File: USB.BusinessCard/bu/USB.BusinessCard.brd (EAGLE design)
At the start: 30.1 x 80 mm, 5 parts

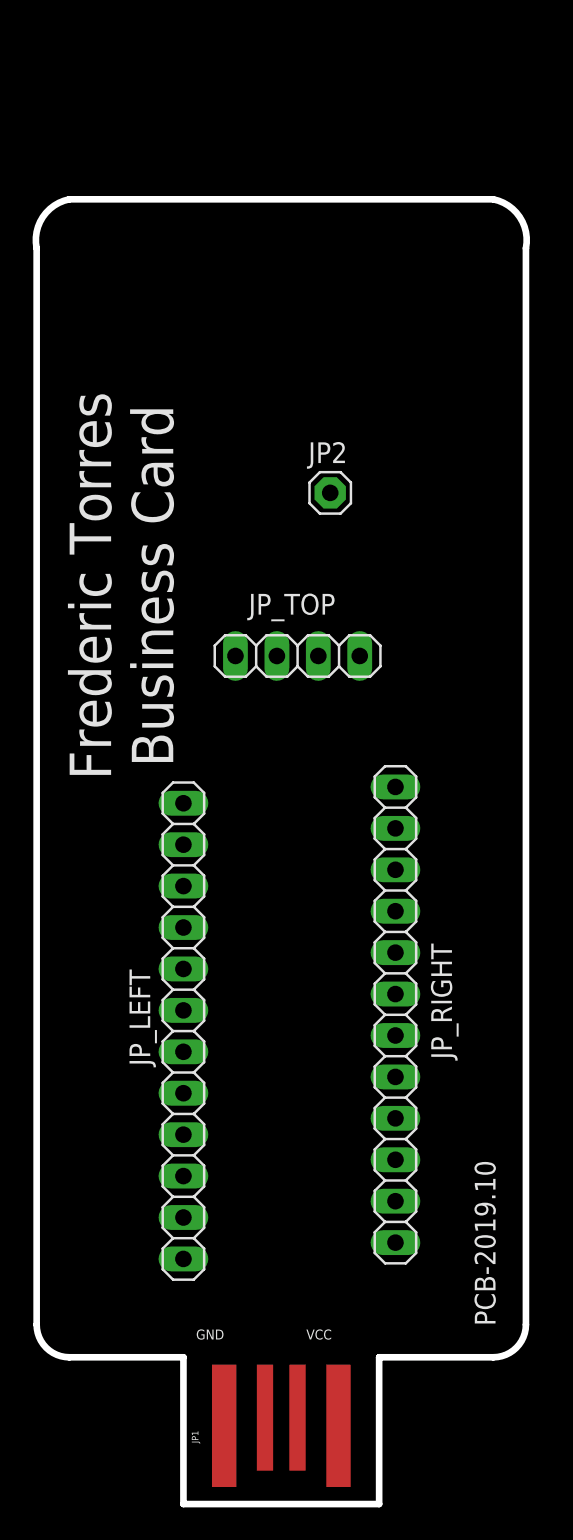
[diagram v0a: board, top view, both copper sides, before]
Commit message: Write firmware for Usb Business Card
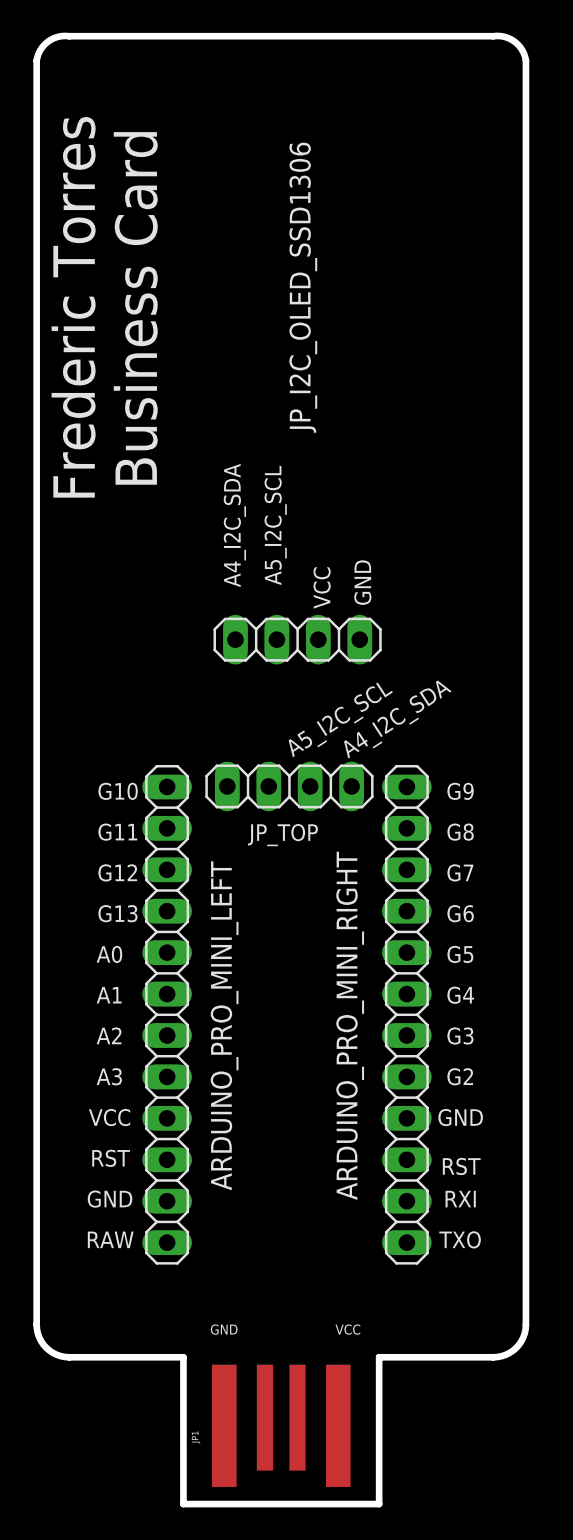
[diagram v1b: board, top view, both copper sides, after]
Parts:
- removed JP2: (no value), adafruit:1X01
- removed JP_LEFT, JP_RIGHT: (no value), adafruit:1X12
- added ARDUINO_PRO_MINI_LEFT, ARDUINO_PRO_MINI_RIGHT: (no value), adafruit:1X12
- added JP_I2C_OLED_SSD1306: (no value), pinhead:1X04
- moved JP_TOP 8.02 mm to (15.5, 44.0)
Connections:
- net A0: now also ARDUINO_PRO_MINI_LEFT.5; no longer JP_LEFT.5
- net A1: now also ARDUINO_PRO_MINI_LEFT.6; no longer JP_LEFT.6
- net A2: now also ARDUINO_PRO_MINI_LEFT.7; no longer JP_LEFT.7
- net A3: now also ARDUINO_PRO_MINI_LEFT.8; no longer JP_LEFT.8
- net A4_I2C_SDA: now also JP_I2C_OLED_SSD1306.4; no longer JP2.1
- net A5_I2C_SCL: now also JP_I2C_OLED_SSD1306.3
- net G10: now also ARDUINO_PRO_MINI_LEFT.1; no longer JP_LEFT.1
- net G11: now also ARDUINO_PRO_MINI_LEFT.2; no longer JP_LEFT.2
- net G12: now also ARDUINO_PRO_MINI_LEFT.3; no longer JP_LEFT.3
- net G13: now also ARDUINO_PRO_MINI_LEFT.4; no longer JP_LEFT.4
- net G2: now also ARDUINO_PRO_MINI_RIGHT.8; no longer JP_RIGHT.8
- net G3: now also ARDUINO_PRO_MINI_RIGHT.7; no longer JP_RIGHT.7
- net G4: now also ARDUINO_PRO_MINI_RIGHT.6; no longer JP_RIGHT.6
- net G5: now also ARDUINO_PRO_MINI_RIGHT.5; no longer JP_RIGHT.5
- net G6: now also ARDUINO_PRO_MINI_RIGHT.4; no longer JP_RIGHT.4
- net G7: now also ARDUINO_PRO_MINI_RIGHT.3; no longer JP_RIGHT.3
- net G8: now also ARDUINO_PRO_MINI_RIGHT.2; no longer JP_RIGHT.2
- net G9: now also ARDUINO_PRO_MINI_RIGHT.1; no longer JP_RIGHT.1
- net GND: now also ARDUINO_PRO_MINI_LEFT.11, ARDUINO_PRO_MINI_RIGHT.9, JP_I2C_OLED_SSD1306.1; no longer JP_LEFT.11, JP_RIGHT.9
- net RAW: now also ARDUINO_PRO_MINI_LEFT.12; no longer JP_LEFT.12
- net RST: now also ARDUINO_PRO_MINI_LEFT.10, ARDUINO_PRO_MINI_RIGHT.10; no longer JP_LEFT.10, JP_RIGHT.10
- net RXI: now also ARDUINO_PRO_MINI_RIGHT.11; no longer JP_RIGHT.11
- net TXO: now also ARDUINO_PRO_MINI_RIGHT.12; no longer JP_RIGHT.12
- net VCC: now also ARDUINO_PRO_MINI_LEFT.9, JP_I2C_OLED_SSD1306.2; no longer JP_LEFT.9
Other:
- board size 30.1 x 80 mm -> 30 x 90 mm
- board text added: "A0"
- board text added: "A1"
- board text added: "A2"
- board text added: "A3"
- board text added: "A4_I2C_SDA"
- board text added: "A5_I2C_SCL"
- board text added: "G10"
- board text added: "G11"
- board text added: "G12"
- board text added: "G13"
- board text added: "G2"
- board text added: "G3"
- board text added: "G4"
- board text added: "G5"
- board text added: "G6"
- board text added: "G7"
- board text added: "G8"
- board text added: "G9"
- board text added: "PCB c 2019.10"
- board text added: "RAW"
- board text added: "RST"
- board text added: "RXI"
- board text added: "TXO"
- board text removed: "Nusbio"
- board text removed: "PCB-2019.10"

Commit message: Update firmware for Usb Business Card
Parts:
- added JP_PROGRAMMING: (no value), adafruit:1X06
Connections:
- removed net G11: ARDUINO_PRO_MINI_LEFT.2
- removed net G12: ARDUINO_PRO_MINI_LEFT.3
- removed net G13: ARDUINO_PRO_MINI_LEFT.4
- new net G11_MOSI: ARDUINO_PRO_MINI_LEFT.2, JP_PROGRAMMING.6
- new net G12_MISO: ARDUINO_PRO_MINI_LEFT.3, JP_PROGRAMMING.5
- new net G13_SCK: ARDUINO_PRO_MINI_LEFT.4, JP_PROGRAMMING.4
- net GND: now also JP_PROGRAMMING.1
- net RST: now also JP_PROGRAMMING.3
- net VCC: now also JP_PROGRAMMING.2
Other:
- board text added: "G11_MOSI"
- board text added: "G12_MISO"
- board text added: "G13_SCK"
- board text removed: "G11"
- board text removed: "G12"
- board text removed: "G13"
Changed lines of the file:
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@@
 <layer number="23" name="tOrigins" color="15" fill="1" visible="yes" active="yes"/>
 <layer number="24" name="bOrigins" color="15" fill="1" visible="yes" active="yes"/>
-<layer number="25" name="tNames" color="7" fill="1" visible="no" active="yes"/>
-<layer number="26" name="bNames" color="7" fill="1" visible="yes" active="yes"/>
+<layer number="25" name="tNames" color="7" fill="1" visible="yes" active="yes"/>
+<layer number="26" name="bNames" color="7" fill="1" visible="no" active="yes"/>
 <layer number="27" name="tValues" color="7" fill="1" visible="yes" active="yes"/>
 <layer number="28" name="bValues" color="7" fill="1" visible="yes" active="yes"/>
@@
 <text x="11.5" y="10.7" size="0.6096" layer="25" rot="R180" align="center">GND</text>
 <text x="19.1" y="10.7" size="0.6096" layer="25" rot="R180" align="center">VCC</text>
-<text x="4.2" y="73.3" size="2.54" layer="25" rot="R90" align="center">Frederic Torres
+<text x="26.2" y="73.3" size="2.54" layer="25" rot="R90" align="center">Frederic Torres
 Business Card</text>
 <text x="15.5" y="20" size="2.54" layer="26" rot="MR270" align="center">MadeInTheUSB.net</text>
@@
 <text x="4.5" y="31.2" size="1.016" layer="25" rot="R180" align="center">A1</text>
 <text x="4.5" y="33.7" size="1.016" layer="25" rot="R180" align="center">A0</text>
-<text x="5" y="36.2" size="1.016" layer="25" rot="R180" align="center">G13</text>
-<text x="5" y="38.7" size="1.016" layer="25" rot="R180" align="center">G12</text>
-<text x="5" y="41.2" size="1.016" layer="25" rot="R180" align="center">G11</text>
+<text x="3.5" y="36.2" size="1.016" layer="25" rot="R180" align="center">G13_SCK</text>
+<text x="3.5" y="38.7" size="0.8128" layer="25" rot="R180" align="center">G12_MISO</text>
+<text x="3.5" y="41.2" size="0.8128" layer="25" rot="R180" align="center">G11_MOSI</text>
 <text x="5" y="43.7" size="1.016" layer="25" rot="R180" align="center">G10</text>
 <text x="26" y="26.2" size="1.016" layer="25" rot="R180" align="center">G2</text>
@@
 <text x="26" y="16.2" size="1.016" layer="25" rot="R180" align="center">TXO</text>
 <text x="4.5" y="16.2" size="1.016" layer="25" rot="R180" align="center">RAW</text>
+<text x="7.5" y="65.7" size="1.016" layer="25" rot="R180" align="center">GND</text>
+<text x="7.5" y="68.2" size="1.016" layer="25" rot="R180" align="center">VCC</text>
+<text x="7.5" y="70.7" size="1.016" layer="25" rot="R180" align="center">RST</text>
+<text x="9" y="73.2" size="1.016" layer="25" rot="R180" align="center">G13_SCK</text>
+<text x="9.5" y="75.7" size="1.016" layer="25" rot="R180" align="center">G12_MISO</text>
+<text x="9.5" y="78.2" size="1.016" layer="25" rot="R180" align="center">G11_MOSI</text>
 </plain>
 <attributes>
@@
 <attribute name="VALUE" x="21.08" y="56.175" size="1.27" layer="27" rot="R180"/>
 </element>
+<element name="JP_PROGRAMMING" library="adafruit" package="1X06" value="" x="4" y="72" smashed="yes" rot="R90">
+<attribute name="NAME" x="2.1712" y="64.3038" size="1.016" layer="25" ratio="10" rot="R90"/>
+<attribute name="VALUE" x="7.175" y="64.38" size="1.27" layer="27" rot="R90"/>
+</element>
 </elements>
 <signals>
@@
 <contactref element="ARDUINO_PRO_MINI_RIGHT" pad="9"/>
 <contactref element="JP_I2C_OLED_SSD1306" pad="1"/>
+<contactref element="JP_PROGRAMMING" pad="1"/>
 <wire x1="22.7" y1="23.65" x2="19.81" y2="53" width="0" layer="19" extent="1-1"/>
 <wire x1="8" y1="18.57" x2="22.7" y2="23.65" width="0" layer="19" extent="1-1"/>
 <wire x1="11.5" y1="4.8" x2="8" y2="18.57" width="0" layer="19" extent="1-1"/>
+<wire x1="4" y1="65.65" x2="11.5" y2="4.8" width="0" layer="19" extent="1-1"/>
 </signal>
 <signal name="VCC">
@@
 <contactref element="ARDUINO_PRO_MINI_LEFT" pad="9"/>
 <contactref element="JP_I2C_OLED_SSD1306" pad="2"/>
+<contactref element="JP_PROGRAMMING" pad="2"/>
 <wire x1="8" y1="23.65" x2="17.27" y2="53" width="0" layer="19" extent="1-1"/>
 <wire x1="18.5" y1="4.8" x2="8" y2="23.65" width="0" layer="19" extent="1-1"/>
+<wire x1="4" y1="68.19" x2="18.5" y2="4.8" width="0" layer="19" extent="1-1"/>
 </signal>
 <signal name="RAW">
@@
 <contactref element="ARDUINO_PRO_MINI_LEFT" pad="10"/>
 <contactref element="ARDUINO_PRO_MINI_RIGHT" pad="10"/>
+<contactref element="JP_PROGRAMMING" pad="3"/>
 <wire x1="8" y1="21.11" x2="22.7" y2="21.11" width="0" layer="19" extent="1-1"/>
+<wire x1="4" y1="70.73" x2="8" y2="21.11" width="0" layer="19" extent="1-1"/>
 </signal>
 <signal name="A3">
@@
 <contactref element="ARDUINO_PRO_MINI_LEFT" pad="5"/>
 </signal>
-<signal name="G13">
+<signal name="G13_SCK">
 <contactref element="ARDUINO_PRO_MINI_LEFT" pad="4"/>
-</signal>
-<signal name="G12">
+<contactref element="JP_PROGRAMMING" pad="4"/>
+<wire x1="8" y1="36.35" x2="4" y2="73.27" width="0" layer="19" extent="1-1"/>
+</signal>
+<signal name="G12_MISO">
 <contactref element="ARDUINO_PRO_MINI_LEFT" pad="3"/>
-</signal>
-<signal name="G11">
+<contactref element="JP_PROGRAMMING" pad="5"/>
+<wire x1="4" y1="75.81" x2="8" y2="38.89" width="0" layer="19" extent="1-1"/>
+</signal>
+<signal name="G11_MOSI">
 <contactref element="ARDUINO_PRO_MINI_LEFT" pad="2"/>
+<contactref element="JP_PROGRAMMING" pad="6"/>
+<wire x1="8" y1="41.43" x2="4" y2="78.35" width="0" layer="19" extent="1-1"/>
 </signal>
 <signal name="G10">

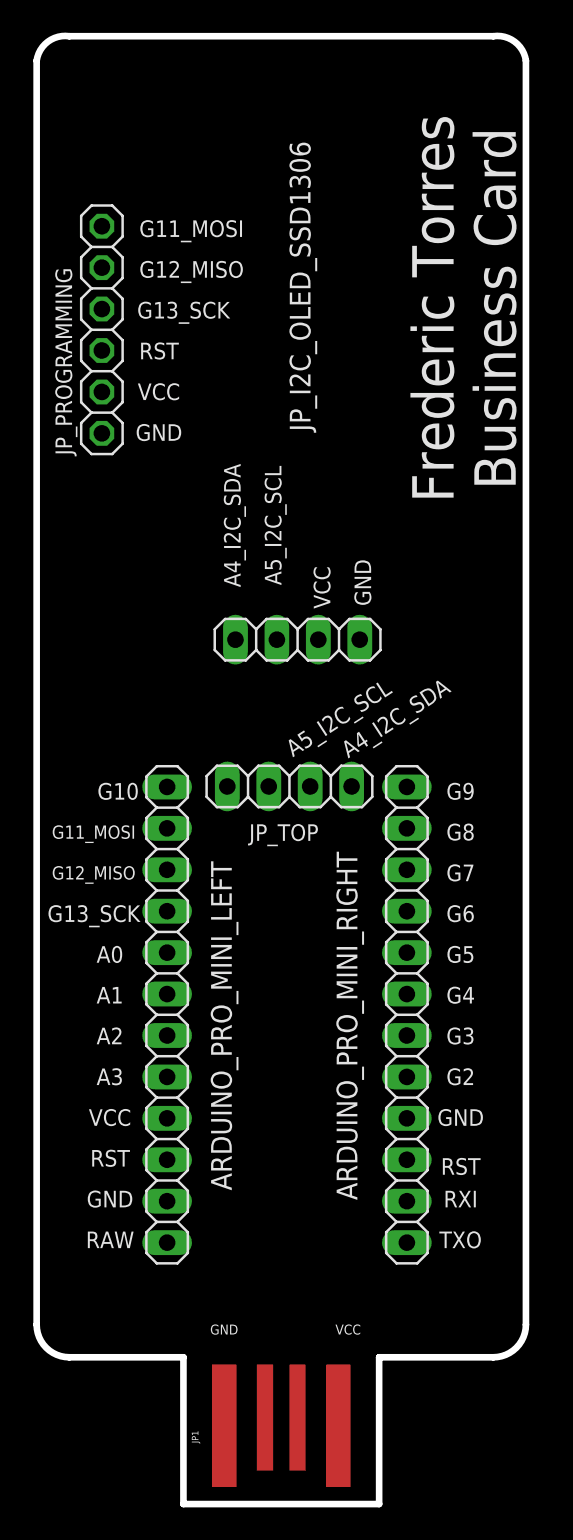
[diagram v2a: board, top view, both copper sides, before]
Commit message: Update firmware for Usb Business Card
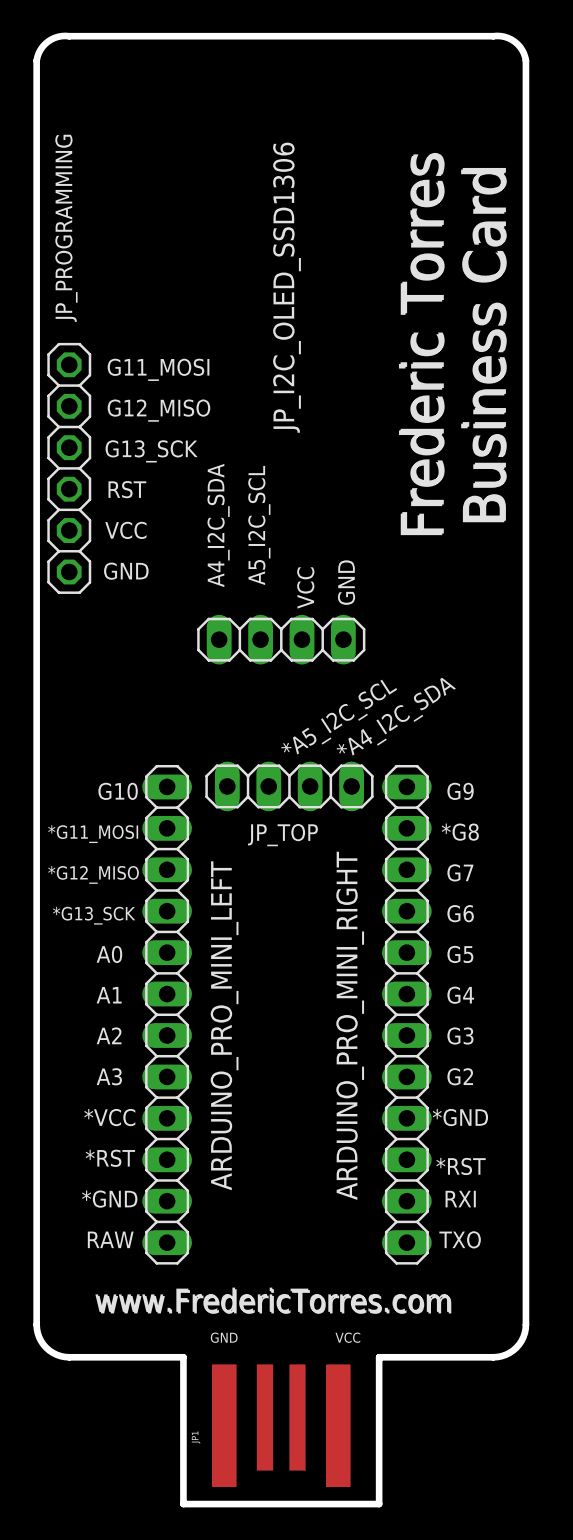
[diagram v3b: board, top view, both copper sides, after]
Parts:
- moved JP_PROGRAMMING 8.73 mm to (2.00, 63.5)
- moved JP_I2C_OLED_SSD1306 1.00 mm to (15.0, 53.0)
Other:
- board text added: "*A4_I2C_SDA"
- board text added: "*A5_I2C_SCL"
- board text added: "*G11_MOSI"
- board text added: "*G12_MISO"
- board text added: "*G13_SCK"
- board text added: "*G8"
- board text added: "*GND"
- board text added: "*RST"
- board text added: "*VCC"
- board text added: "PCB v 2019.10"
- board text added: "www.FredericTorres.com"
- board text removed: "G8"
- board text removed: "MadeInTheUSB.net"
- board text removed: "PCB c 2019.10"
